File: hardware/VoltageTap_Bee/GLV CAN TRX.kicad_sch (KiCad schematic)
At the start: 10 parts, among them J3 Conn_01x04_Socket, U10 MCP2542FDxMF, U4 RAA211805, U5 STISO620

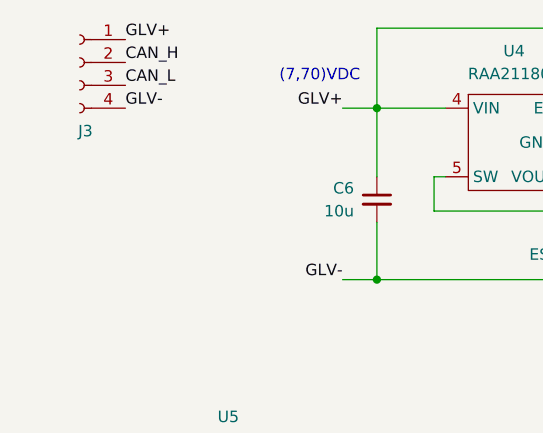
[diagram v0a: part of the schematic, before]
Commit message: VT_BEE changes
need to somehow fit switches, make space
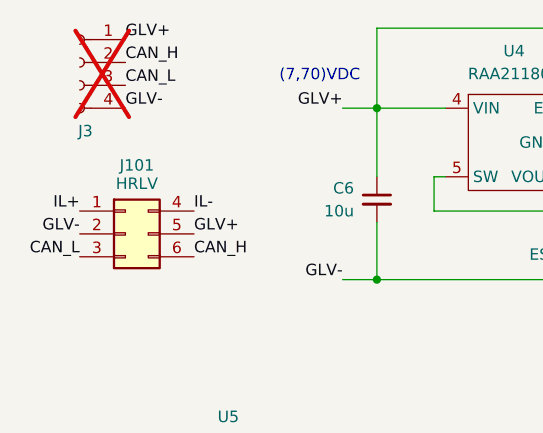
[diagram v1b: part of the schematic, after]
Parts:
- added J101: HRLV, Connector_Molex:Molex_Micro-Fit_3.0_43045-0600_2x03_P3.00mm_Horizontal, symbol Connector_Generic:Conn_02x03_Top_Bottom
- J3: now not fitted
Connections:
- net CAN_H: now also J101.6 (Pin_6)
- net CAN_L: now also J101.3 (Pin_3)
- net GLV+: now also J101.5 (Pin_5)
- net GLV-: now also J101.2 (Pin_2)
- new net IL+: J101.1 (Pin_1)
- new net IL-: J101.4 (Pin_4)
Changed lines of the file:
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@@
+		)
+	)
+	(label "CAN_L"
+		(at 21.59 46.99 180)
+		(effects
+			(font
+				(size 1.27 1.27)
+			)
+			(justify right bottom)
+		)
+	)
+	(label "GLV-"
+		(at 21.59 44.45 180)
+		(effects
+			(font
+				(size 1.27 1.27)
+			)
+			(justify right bottom)
 		)
 	)
@@
 		)
 	)
+	(label "GLV+"
+		(at 34.29 44.45 0)
+		(effects
+			(font
+				(size 1.27 1.27)
+			)
+			(justify left bottom)
+		)
+	)
 	(label "5v"
 		(at 111.76 67.31 0)
@@
 		)
 	)
+	(label "IL+"
+		(at 21.59 41.91 180)
+		(effects
+			(font
+				(size 1.27 1.27)
+			)
+			(justify right bottom)
+		)
+	)
 	(label "CAN_H"
 		(at 26.67 25.4 0)
@@
 		)
 	)
+	(label "IL-"
+		(at 34.29 41.91 0)
+		(effects
+			(font
+				(size 1.27 1.27)
+			)
+			(justify left bottom)
+		)
+	)
 	(label "GLV+"
 		(at 26.67 22.86 0)
@@
 	(label "GLV-"
 		(at 101.6 49.53 0)
+		(effects
+			(font
+				(size 1.27 1.27)
+			)
+			(justify left bottom)
+		)
+	)
+	(label "CAN_H"
+		(at 34.29 46.99 0)
 		(effects
 			(font
@@
 		(exclude_from_sim no)
 		(in_bom yes)
-		(on_board yes)
-		(dnp no)
+		(on_board no)
+		(dnp yes)
 		(property "Reference" "J3"
 			(at 22.225 33.02 0)
@@
 					(unit 1)
 				)
+			)
+		)
+	)
+	(symbol
+		(lib_id "Connector_Generic:Conn_02x03_Top_Bottom")
+		(at 26.67 44.45 0)
+		(unit 1)
+		(exclude_from_sim no)
+		(in_bom yes)
+		(on_board yes)
+		(dnp no)
+		(property "Reference" "J101"
+			(at 27.94 36.83 0)
+			(effects
+				(font
+					(size 1.27 1.27)
+				)
+			)
+		)
+		(property "Value" "HRLV"
+			(at 27.94 38.862 0)
+			(effects
+				(font
+					(size 1.27 1.27)
+				)
+			)
+		)
+		(property "Footprint" "Connector_Molex:Molex_Micro-Fit_3.0_43045-0600_2x03_P3.00mm_Horizontal"
+			(at 26.67 44.45 0)
+			(effects
+				(font
+					(size 1.27 1.27)
+				)
+				(hide yes)
+			)
+		)
+		(property "Datasheet" "~"
+			(at 26.67 44.45 0)
+			(effects
+				(font
+					(size 1.27 1.27)
+				)
+				(hide yes)
+			)
+		)
+		(property "Description" "Generic connector, double row, 02x03, top/bottom pin numbering scheme (row 1: 1...pins_per_row, row2: pins_per_row+1 ... num_pins), script generated (kicad-library-utils/schlib/autogen/connector/)"
+			(at 26.67 44.45 0)
+			(effects
+				(font
+					(size 1.27 1.27)
+				)
+				(hide yes)
+			)
+		)
+		(property "mouser" "https://www.mouser.com/ProductDetail/Molex/43045-0612?qs=KC2ywxza1kqWo9LLJ5Lh3w%3D%3D"
+			(at 26.67 44.45 0)
+			(effects
+				(font
+					(size 1.27 1.27)
+				)
+				(hide yes)
+			)
+		)
+		(property "unit x10" "0.721"
+			(at 26.67 44.45 0)
+			(effects
+				(font
+					(size 1.27 1.27)
+				)
+				(hide yes)
+			)
+		)
+		(property "unit x1" "0.85"
+			(at 26.67 44.45 0)
+			(effects
+				(font
+					(size 1.27 1.27)
+				)
+				(hide yes)
+			)
+		)
+		(property "Sim.Pins" ""
+			(at 26.67 44.45 0)
+			(effects
+				(font
+					(size 1.27 1.27)
+				)
+				(hide yes)
+			)
+		)
+		(property "note" ""
+			(at 26.67 44.45 0)
+			(effects
+				(font
+					(size 1.27 1.27)
+				)
+				(hide yes)
+			)
+		)
+		(pin "5"
+		)
+		(pin "6"
+		)
+		(pin "1"
+		)
+		(pin "2"
+		)
+		(pin "3"
+		)
+		(pin "4"
+		)
+		(instances
+			(project "VoltageTap_B"
+				(path "/24c6cb45-cbeb-4148-a23c-ec2e76234670/443e7a8e-9df5-428f-9d56-3f2b4e9a9ffe"
+					(reference "J101")
+					(unit 1)
+				)

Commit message: uhhh part 2
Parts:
- removed C10, C6: 10u, Capacitor_SMD:C_1206_3216Metric_Pad1.33x1.80mm_HandSolder, symbol Device:C_Small
- removed D2: ES1D, Diode_SMD:D_SMA, symbol Device:D_Schottky_Small
- removed L1: 22u, Inductor_SMD:L_1210_3225Metric_Pad1.42x2.65mm_HandSolder, symbol Device:L_Small
- removed R16: 200k, Resistor_SMD:R_0805_2012Metric_Pad1.20x1.40mm_HandSolder, symbol Device:R_Small_US
- removed U4: RAA211805, Package_TO_SOT_SMD:TSOT-23-5, symbol zzLocalLibrary:RAA211805
- added U27: AP7384-50SA, Package_TO_SOT_SMD:SOT-23, symbol Regulator_Linear:AP7384-50SA
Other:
- note removed: "(7,70)VDC"

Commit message: nlaeclnaec
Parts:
- removed R23: 200k, Resistor_SMD:R_0805_2012Metric_Pad1.20x1.40mm_HandSolder, symbol Device:R_Small_US
- added C301, C302: 220n, Capacitor_SMD:C_0805_2012Metric_Pad1.18x1.45mm_HandSolder, symbol Device:C_Small
- added CR301: ESD2CAN36DBZRQ1, Package_TO_SOT_SMD:TSOT-23_HandSoldering, symbol zzLocalLibrary:ESD2CAN36DBZRQ1
- added D301: ES1D, Diode_SMD:D_SMA, symbol Device:D_Schottky_Small
- added FL301: Choke_CommonMode_FerriteCore_1243, Inductor_SMD:L_CommonModeChoke_Coilcraft_1812CAN, symbol Filter:Choke_CommonMode_FerriteCore_1243
- added U301: ISO1044BD, Package_SO:SOIC-8_5.3x5.3mm_P1.27mm, symbol Interface_CAN_LIN:ISO1044BD
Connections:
- net 5v: now also U27.2 (VO), C301.1, U301.8 (VCC2)
- net GLV-: now also CR301.3 (GND), U301.7 (GND2)
- net at U27.1 (VI): now also C302.1
- net at U27.3 (GND): now also C301.2, C302.2
- new net: CR301.2 (IO), FL301.3, U301.5 (CANL)
- new net: CR301.1 (IO), FL301.2, U301.6 (CANH)

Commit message: lnaecnlaec
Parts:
- added K301: G5Q-1A 24Vdc, Relay_THT:Relay_SPST_Omron-G5Q-1A, symbol Relay:G5Q-1A
- added Q301: TSM2328CX, Package_TO_SOT_SMD:SOT-23-3, symbol Transistor_FET:Q_NMOS_GSD
- added U302: ISOM8110DFS, zzLocalLibraries-Footprints:ISOM811_SOIC-4_DFG, symbol zzLocalLibrary:ISOM811_0_3

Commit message: vssv
sdvsv
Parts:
- removed K301: G5Q-1A 24Vdc, Relay_THT:Relay_SPST_Omron-G5Q-1A, symbol Relay:G5Q-1A
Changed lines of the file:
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@@
-	)
-	(symbol
-		(lib_id "Relay:G5Q-1A")
-		(at 121.92 123.19 90)
-		(mirror x)
-		(unit 1)
-		(exclude_from_sim no)
-		(in_bom yes)
-		(on_board yes)
-		(dnp no)
-		(property "Reference" "K301"
-			(at 121.92 135.0518 90)
-			(effects
-				(font
-					(size 1.27 1.27)
-				)
-			)
-		)
-		(property "Value" "G5Q-1A 24Vdc"
-			(at 121.92 132.7404 90)
-			(effects
-				(font
-					(size 1.27 1.27)
-				)
-			)
-		)
-		(property "Footprint" "Relay_THT:Relay_SPST_Omron-G5Q-1A"
-			(at 123.19 132.08 0)
-			(effects
-				(font
-					(size 1.27 1.27)
-				)
-				(justify left)
-				(hide yes)
-			)
-		)
-		(property "Datasheet" "https://www.omron.com/ecb/products/pdf/en-g5q.pdf"
-			(at 121.92 123.19 0)
-			(effects
-				(font
-					(size 1.27 1.27)
-				)
-				(hide yes)
-			)
-		)
-		(property "Description" ""
-			(at 121.92 123.19 0)
-			(effects
-				(font
-					(size 1.27 1.27)
-				)
-				(hide yes)
-			)
-		)
-		(property "specs" "24V drive"
-			(at 121.92 123.19 90)
-			(effects
-				(font
-					(size 1.27 1.27)
-				)
-				(hide yes)
-			)
-		)
-		(property "mouser" "https://www.mouser.com/ProductDetail/Omron-Electronics/G5Q-1A-EU-DC24?qs=jvGqVfHPSOIMrQJAl4KV5Q%3D%3D"
-			(at 121.92 123.19 90)
-			(effects
-				(font
-					(size 1.27 1.27)
-				)
-				(hide yes)
-			)
-		)
-		(property "unit x10" "1.53"
-			(at 121.92 123.19 90)
-			(effects
-				(font
-					(size 1.27 1.27)
-				)
-				(hide yes)
-			)
-		)
-		(property "unit x1" "1.70"
-			(at 121.92 123.19 90)
-			(effects
-				(font
-					(size 1.27 1.27)
-				)
-				(hide yes)
-			)
-		)
-		(property "Sim.Pins" ""
-			(at 121.92 123.19 90)
-			(effects
-				(font
-					(size 1.27 1.27)
-				)
-				(hide yes)
-			)
-		)
-		(property "note" ""
-			(at 121.92 123.19 90)
-			(effects
-				(font
-					(size 1.27 1.27)
-				)
-				(hide yes)
-			)
-		)
-		(pin "1"
-		)
-		(pin "2"
-		)
-		(pin "3"
-		)
-		(pin "5"
-		)
-		(instances
-			(project "VoltageTap_B"
-				(path "/24c6cb45-cbeb-4148-a23c-ec2e76234670/443e7a8e-9df5-428f-9d56-3f2b4e9a9ffe"
-					(reference "K301")
-					(unit 1)
-				)
-			)
-		)
 	)
 	(symbol

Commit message: baeckbjlnacnklac
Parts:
- renumbered C302 to C301, C301 to C302, J3 to J301, J101 to J302, U5 to U301, U301 to U302, U10 to U303, U27 to U304, U302 to U305
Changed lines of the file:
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@@
 		(on_board yes)
 		(dnp no)
-		(property "Reference" "C302"
+		(property "Reference" "C301"
 			(at 71.12 35.5662 0)
 			(effects
@@
 			(project "VoltageTap_B"
 				(path "/24c6cb45-cbeb-4148-a23c-ec2e76234670/443e7a8e-9df5-428f-9d56-3f2b4e9a9ffe"
-					(reference "C302")
+					(reference "C301")
 					(unit 1)
 				)
@@
 		(dnp no)
 		(fields_autoplaced yes)
-		(property "Reference" "U302"
+		(property "Reference" "U305"
 			(at 142.875 120.65 0)
 			(effects
@@
 			(project "VoltageTap_B"
 				(path "/24c6cb45-cbeb-4148-a23c-ec2e76234670/443e7a8e-9df5-428f-9d56-3f2b4e9a9ffe"
-					(reference "U302")
+					(reference "U305")
 					(unit 1)
 				)
@@
 		(dnp no)
 		(fields_autoplaced yes)
-		(property "Reference" "U27"
+		(property "Reference" "U304"
 			(at 85.09 25.4 0)
 			(effects
@@
 			(project "VoltageTap_B"
 				(path "/24c6cb45-cbeb-4148-a23c-ec2e76234670/443e7a8e-9df5-428f-9d56-3f2b4e9a9ffe"
-					(reference "U27")
+					(reference "U304")
 					(unit 1)
 				)
@@
 		(on_board yes)
 		(dnp no)
-		(property "Reference" "U301"
+		(property "Reference" "U302"
 			(at 57.15 162.56 0)
 			(effects
@@
 			(project "VoltageTap_B"
 				(path "/24c6cb45-cbeb-4148-a23c-ec2e76234670/443e7a8e-9df5-428f-9d56-3f2b4e9a9ffe"
-					(reference "U301")
+					(reference "U302")
 					(unit 1)
 				)
@@
 		(on_board yes)
 		(dnp no)
-		(property "Reference" "C301"
+		(property "Reference" "C302"
 			(at 99.06 34.2962 0)
 			(effects
@@
 			(project "VoltageTap_B"
 				(path "/24c6cb45-cbeb-4148-a23c-ec2e76234670/443e7a8e-9df5-428f-9d56-3f2b4e9a9ffe"
-					(reference "C301")
+					(reference "C302")
 					(unit 1)
 				)
@@
 		(dnp no)
 		(fields_autoplaced yes)
-		(property "Reference" "U5"
+		(property "Reference" "U301"
 			(at 38.1 64.77 0)
 			(effects
@@
 			(project "VoltageTap_B"
 				(path "/24c6cb45-cbeb-4148-a23c-ec2e76234670/443e7a8e-9df5-428f-9d56-3f2b4e9a9ffe"
-					(reference "U5")
+					(reference "U301")
 					(unit 1)
 				)
@@
 		(dnp no)
 		(fields_autoplaced yes)
-		(property "Reference" "U10"
+		(property "Reference" "U303"
 			(at 79.6133 88.9 0)
 			(effects
@@
 			(project "VoltageTap_B"
 				(path "/24c6cb45-cbeb-4148-a23c-ec2e76234670/443e7a8e-9df5-428f-9d56-3f2b4e9a9ffe"
-					(reference "U10")
+					(reference "U303")
 					(unit 1)
 				)
@@
 		(on_board no)
 		(dnp yes)
-		(property "Reference" "J3"
+		(property "Reference" "J301"
 			(at 22.225 33.02 0)
 			(effects
@@
 			(project "VoltageTap_B"
 				(path "/24c6cb45-cbeb-4148-a23c-ec2e76234670/443e7a8e-9df5-428f-9d56-3f2b4e9a9ffe"
-					(reference "J3")
+					(reference "J301")
 					(unit 1)
 				)
@@
 		(on_board yes)
 		(dnp no)
-		(property "Reference" "J101"
+		(property "Reference" "J302"
 			(at 27.94 36.83 0)
 			(effects
@@
 			(project "VoltageTap_B"
 				(path "/24c6cb45-cbeb-4148-a23c-ec2e76234670/443e7a8e-9df5-428f-9d56-3f2b4e9a9ffe"
-					(reference "J101")
+					(reference "J302")
 					(unit 1)
 				)

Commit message: schematic updates
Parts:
- removed Q301: TSM2328CX, Package_TO_SOT_SMD:SOT-23-3, symbol Transistor_FET:Q_NMOS_GSD
- removed U301: STISO620, Package_SO:SOIC-8_7.5x5.85mm_P1.27mm, symbol zzLocalLibrary:STISO621
- removed U303: MCP2542FDxMF, Package_SO:JEITA_SOIC-8_3.9x4.9mm_P1.27mm, symbol Interface_CAN_LIN:MCP2542FDxMF
- removed U305: ISOM8110DFS, zzLocalLibraries-Footprints:ISOM811_SOIC-4_DFG, symbol zzLocalLibrary:ISOM811_0_3
- added D2: green, LED_SMD:LED_0805_2012Metric_Pad1.15x1.40mm_HandSolder, symbol Device:LED_Small
- added J1: Conn_01x04_Pin, Connector_PinHeader_2.54mm:PinHeader_1x04_P2.54mm_Vertical, symbol Connector:Conn_01x04_Pin
- added R5: 750, Resistor_SMD:R_1206_3216Metric_Pad1.30x1.75mm_HandSolder, symbol Device:R_Small_US
- added R6: 2.4k, Resistor_SMD:R_0805_2012Metric_Pad1.20x1.40mm_HandSolder, symbol Device:R_Small_US
- added U2: STISO620, Package_SO:SOIC-8_7.5x5.85mm_P1.27mm, symbol zzLocalLibrary:STISO621
- added U3: ISOM8110DFS, zzLocalLibraries-Footprints:ISOM811_SOIC-4_DFG, symbol zzLocalLibrary:ISOM811_0_3
- added U4: TLP176AM, Package_SO:Toshiba_SOIC-4-6_4.4x3.6mm_P1.27mm, symbol Relay_SolidState:TLP175A
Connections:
- net 5v: now also R6.2
- net CAN_H: now also FL301.1
- net CAN_L: now also FL301.4
- net GLV+: now also D301.2 (A)
- net GLV-: now also D2.1 (K), J1.4 (Pin_4), U2.5 (GND2)
- net IL+: now also U4.6
- net IL-: now also U4.4
- net VDD: now also U302.1 (VCC1), U2.1 (VDD1)
- net VSS: now also U302.4 (GND1), U2.4 (GND1), U3.2 (-TX)
- net at C301.1, U304.1 (VI): now also D301.1 (K)
- net CAN_TXD: now reaches U302.2 (TXD)
- net CAN_RXD: now reaches U302.3 (RXD)
- new net: R5.2, U3.1 (+TX)
- new net: U3.3 (E), U4.1
- new net: R6.1, U3.4 (C)
- new net: D2.2 (A), U4.3
- new net 3v3: J1.1 (Pin_1), U2.8 (VDD2)
- new net IL_EN: R5.1
- new net UART_RX: J1.2 (Pin_2), U2.7 (TXB)
- new net UART_RXD: U2.2 (RXB)
- new net UART_TX: J1.3 (Pin_3), U2.6 (RXA)
- new net UART_TXD: U2.3 (TXA)
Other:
- note added: "CAN"
- note added: "Isolated UART Connection"
- note removed: "symbol has 9 pins, but pin 9 is identical to pin 2"
- moved on the sheet: C301, C302, CR301, D301, FL301, U302, U304

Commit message: vt cleaned kinda.
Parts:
- added Q301: MMBT5550L, Package_TO_SOT_SMD:SOT-23, symbol Transistor_BJT:MMBT5550L
- added R301: 226, Resistor_SMD:R_0805_2012Metric_Pad1.20x1.40mm_HandSolder, symbol Device:R_Small_US
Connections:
- net 5v: now also U3.4 (C), Q301.3 (C); no longer R6.2
- net GLV-: now also U4.3; no longer J1.4 (Pin_4), U2.5 (GND2)
- net at U3.3 (E): now also R6.2, Q301.1 (B); no longer U4.1
- net at R6.1: now also D2.2 (A); no longer U3.4 (C)
- net 3v3 renamed UART+
- new net: Q301.2 (E), R301.1
- new net: R301.2, U4.1
- new net UART-: J1.4 (Pin_4), U2.5 (GND2)
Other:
- moved on the sheet: D2, J1, R6, U4
